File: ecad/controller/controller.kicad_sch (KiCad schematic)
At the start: 19 parts, among them J1 Conn_01x03_Pin, P1 USB_C_Plug_USB2.0, SW1 RST, SW2 BOOT, SW3 USER1, SW4 USER2, U1 ESP32-S3-WROOM-1, U2 AMS1117-3.3, U3 SN74LVC1T45DBV

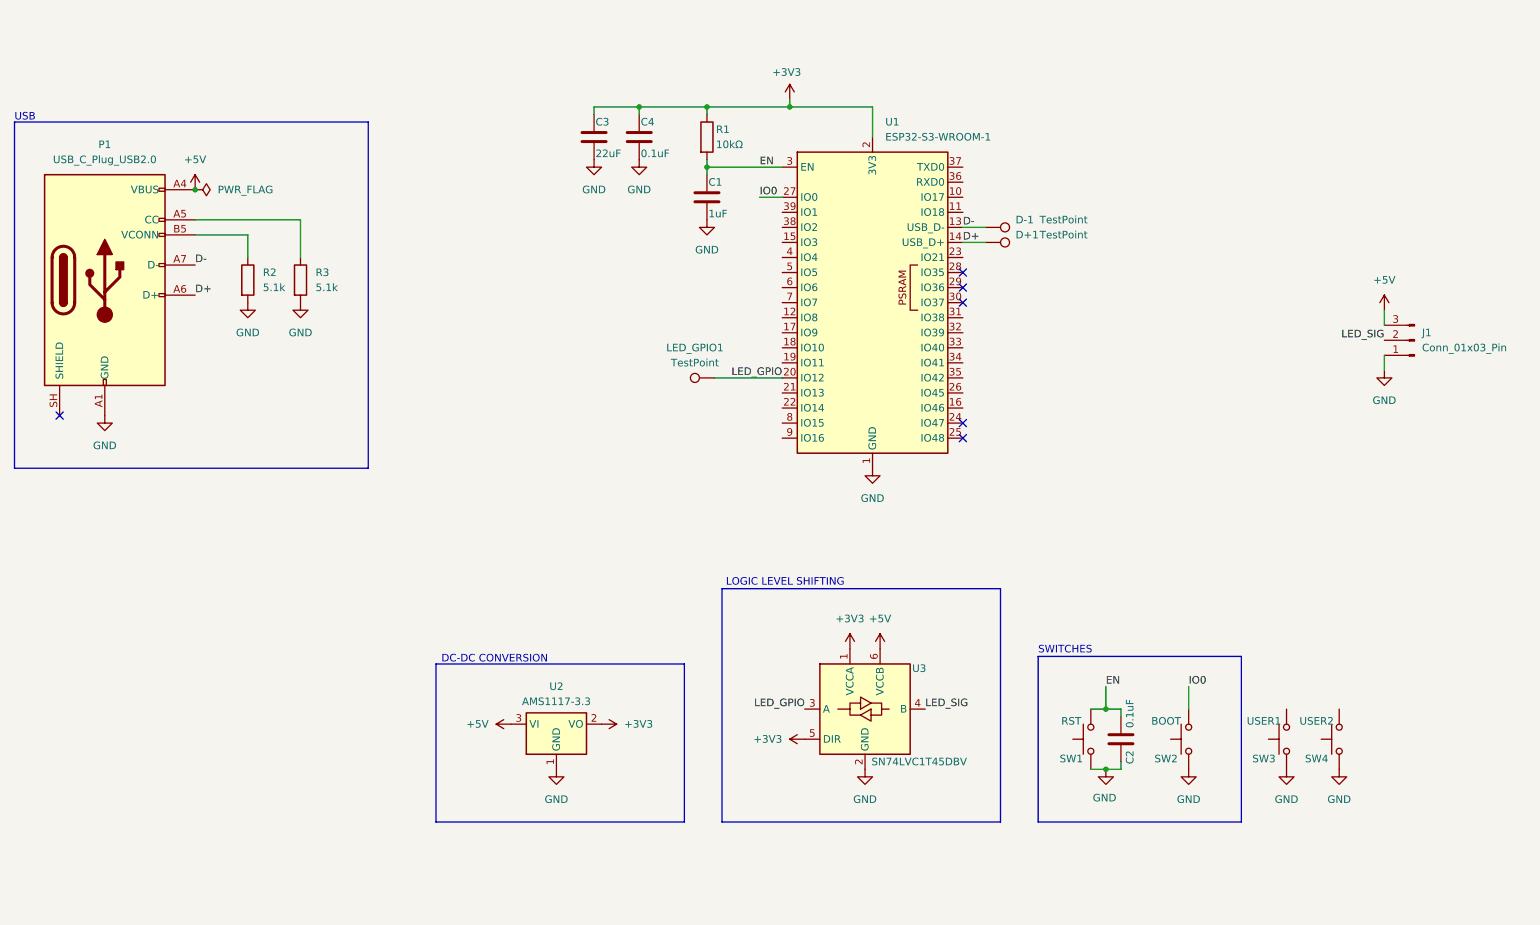
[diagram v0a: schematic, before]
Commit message: split into 2 boards; switch led panel from 4 layers to 2 layers;
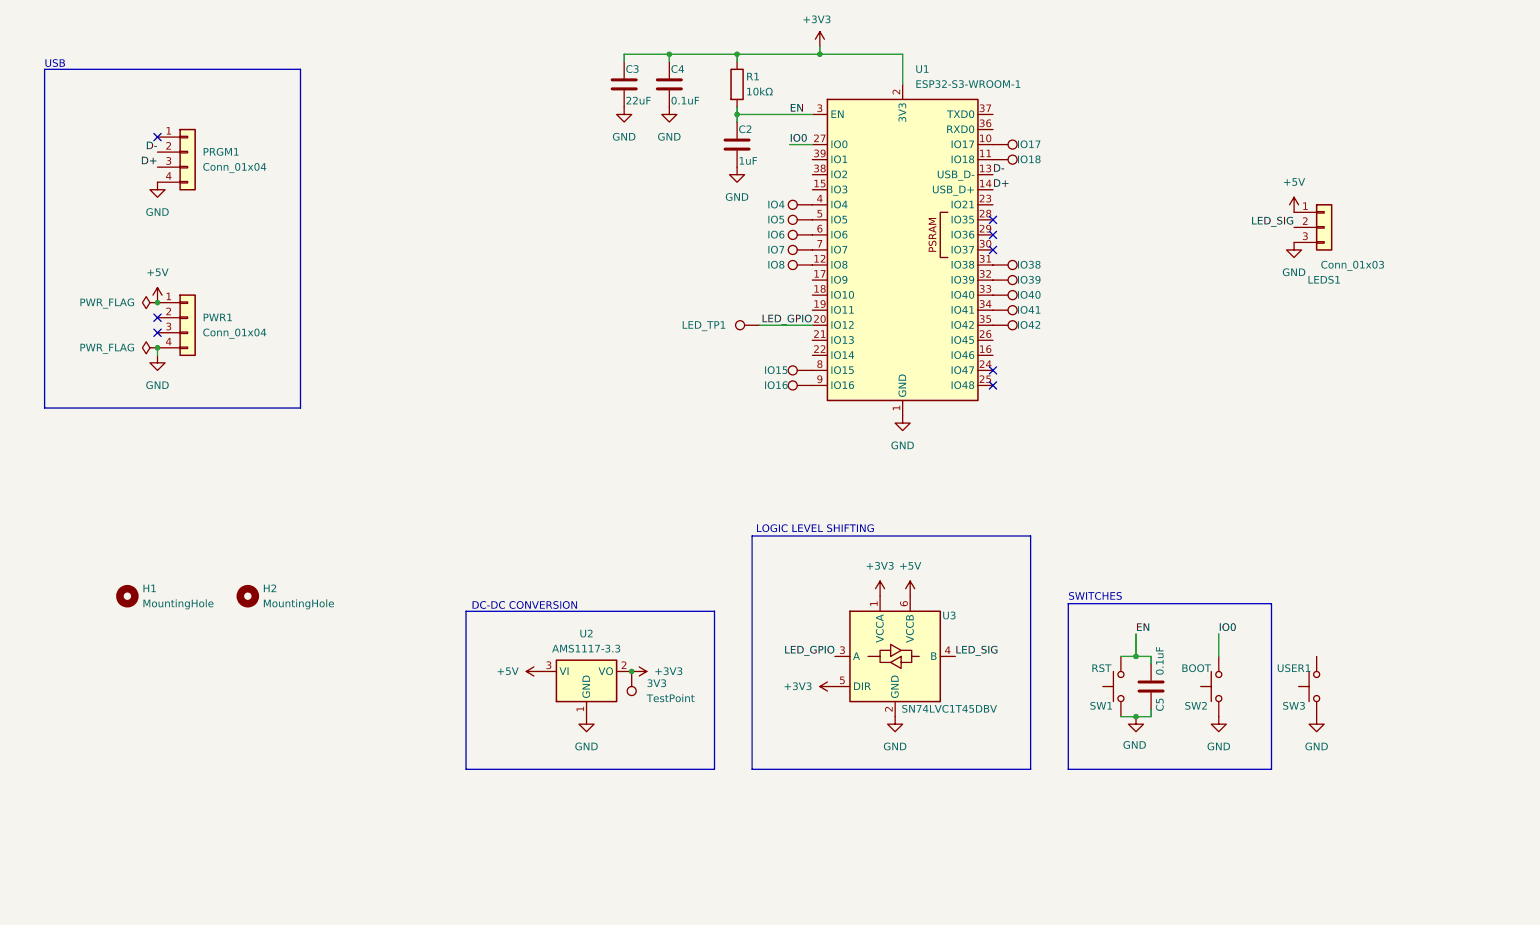
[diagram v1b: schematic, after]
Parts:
- removed C1: 1uF, Capacitor_SMD:C_0805_2012Metric, symbol Device:C
- removed D+1, D-1, LED_GPIO1: TestPoint, symbol Connector:TestPoint
- removed J1: Conn_01x03_Pin, symbol Connector:Conn_01x03_Pin
- removed P1: USB_C_Plug_USB2.0, Connector_USB:USB_C_Receptacle_HRO_TYPE-C-31-M-17, symbol Connector:USB_C_Plug_USB2.0
- removed R2, R3: 5.1k, Resistor_SMD:R_0805_2012Metric, symbol Device:R
- removed SW4: USER2, Button_Switch_THT:SW_PUSH_6mm, symbol Switch:SW_Push
- added 3V3, IO15, IO16, IO17, IO18, IO38, IO39, IO4, IO40, IO41, IO42, IO5, IO6, IO7, IO8, LED_TP1: TestPoint, TestPoint:TestPoint_Pad_D1.5mm, symbol Connector:TestPoint
- added C5: 0.1uF, Capacitor_SMD:C_0805_2012Metric, symbol Device:C
- added H1, H2: MountingHole, MountingHole:MountingHole_3.2mm_M3_Pad, symbol Mechanical:MountingHole
- added LEDS1: Conn_01x03, Connector_JST:JST_XH_B3B-XH-AM_1x03_P2.50mm_Vertical, symbol Connector_Generic:Conn_01x03
- added PRGM1, PWR1: Conn_01x04, Connector_JST:JST_XH_B4B-XH-AM_1x04_P2.50mm_Vertical, symbol Connector_Generic:Conn_01x04
- C2: value 0.1uF -> 1uF; KiLib_Generator (none) -> SMD_2terminal_chip_molded
- C3, C4, R1: KiLib_Generator (none) -> SMD_2terminal_chip_molded
- SW1, SW2: footprint Button_Switch_THT:SW_PUSH_6mm -> Button_Switch_SMD:SW_SPST_TS-1088-xR020
- SW3: footprint Button_Switch_THT:SW_PUSH_6mm -> Connector_JST:JST_XH_B3B-XH-AM_1x03_P2.50mm_Vertical; KiLib_Generator (none) -> connector/JST
- U3: KiLib_Generator (none) -> package/gullwing
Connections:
- net +3V3: now also 3V3.1
- net +5V: now also LEDS1.1 (Pin_1), PWR1.1 (Pin_1)
- net D+: now also PRGM1.3 (Pin_3)
- net D-: now also PRGM1.2 (Pin_2)
- net EN: now also C5.1
- net GND: now also C5.2, LEDS1.3 (Pin_3), PRGM1.4 (Pin_4), PWR1.4 (Pin_4)
- net LED_GPIO: now also LED_TP1.1
- net LED_SIG: now also LEDS1.2 (Pin_2)
- net at U1.10 (IO17): now also IO17.1
- net at U1.11 (IO18): now also IO18.1
- net at U1.12 (IO8): now also IO8.1
- net at U1.31 (IO38): now also IO38.1
- net at U1.32 (IO39): now also IO39.1
- net at U1.33 (IO40): now also IO40.1
- net at U1.34 (IO41): now also IO41.1
- net at U1.35 (IO42): now also IO42.1
- net at U1.4 (IO4): now also IO4.1
- net at U1.5 (IO5): now also IO5.1
- net at U1.6 (IO6): now also IO6.1
- net at U1.7 (IO7): now also IO7.1
- net at U1.8 (IO15): now also IO15.1
- net at U1.9 (IO16): now also IO16.1
- no-connect marks 6 -> 8

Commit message: added vertical USB-C connector to controller board; and possibly much more
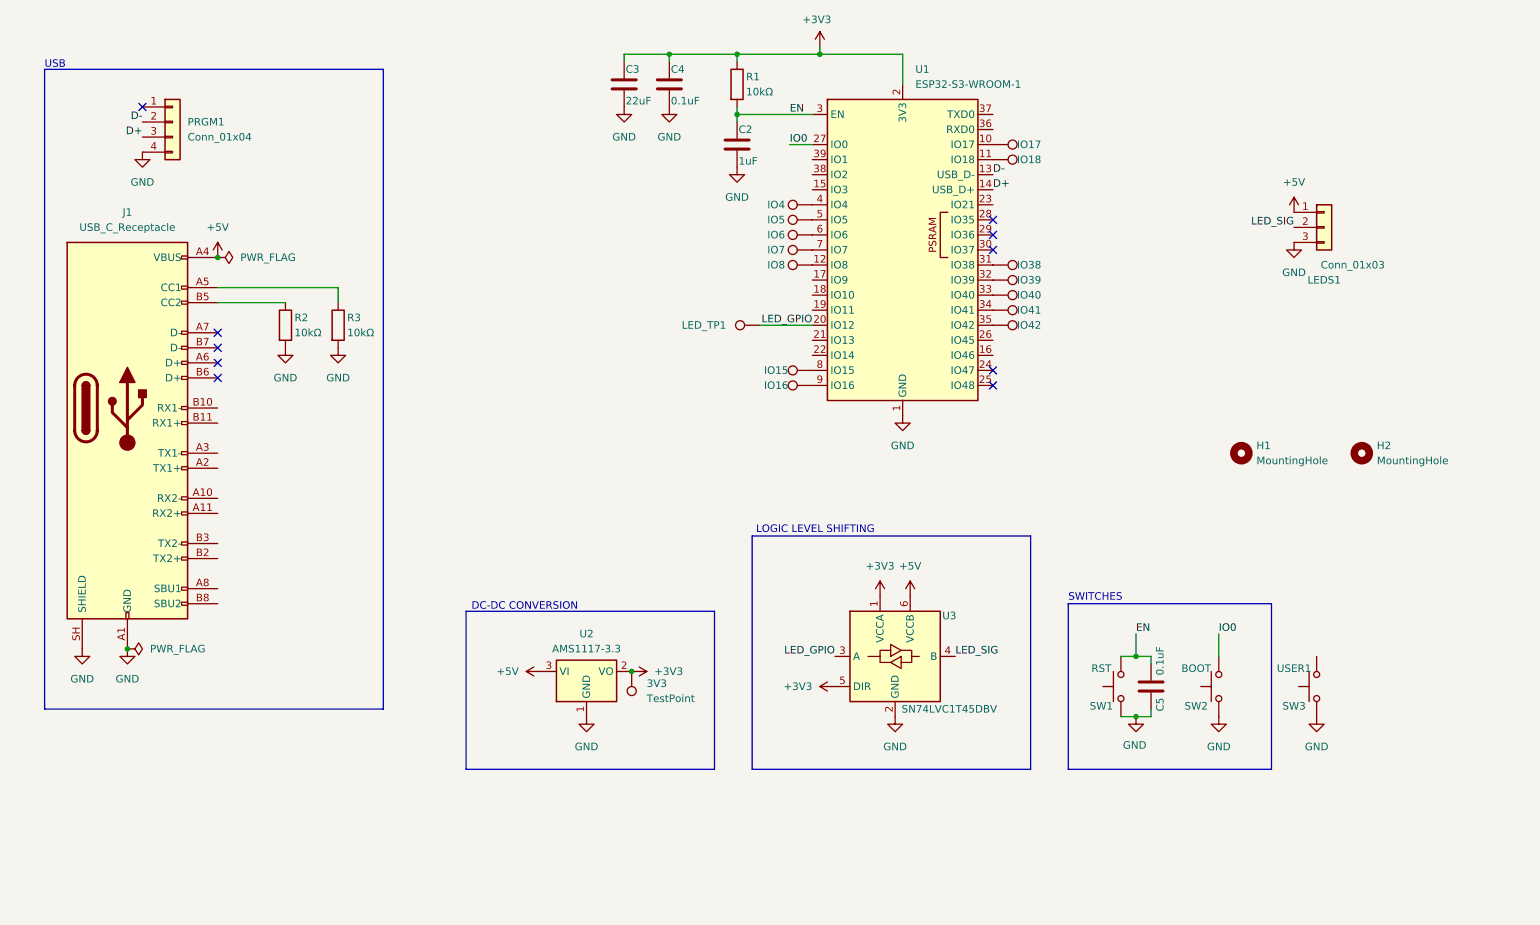
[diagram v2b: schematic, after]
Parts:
- removed PWR1: Conn_01x04, Connector_JST:JST_XH_B4B-XH-AM_1x04_P2.50mm_Vertical, symbol Connector_Generic:Conn_01x04
- added J1: USB_C_Receptacle, usb-library:USB-C-VERTICAL-14P, symbol Connector:USB_C_Receptacle
- added R2, R3: 10kΩ, Resistor_SMD:R_0805_2012Metric, symbol Device:R
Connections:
- net +5V: now also J1.A4 (VBUS), J1.A9 (VBUS), J1.B4 (VBUS), J1.B9 (VBUS)
- net GND: now also J1.A1 (GND), J1.A12 (GND), J1.B1 (GND), J1.B12 (GND), J1.SH (SHIELD), R2.2, R3.2
- new net: J1.A5 (CC1), R3.1
- new net: J1.B5 (CC2), R2.1
- no-connect marks 8 -> 10
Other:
- moved on the sheet: H1, H2, PRGM1

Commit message: who knows
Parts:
- SW3: footprint Connector_JST:JST_XH_B3B-XH-AM_1x03_P2.50mm_Vertical -> Button_Switch_SMD:SW_Push_1P1T_NO_E-Switch_TL3301NxxxxxG
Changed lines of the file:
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@@
 			)
 		)
-		(property "Footprint" "Connector_JST:JST_XH_B3B-XH-AM_1x03_P2.50mm_Vertical"
+		(property "Footprint" "Button_Switch_SMD:SW_Push_1P1T_NO_E-Switch_TL3301NxxxxxG"
 			(at 237.49 137.16 0)
 			(hide yes)

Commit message: add ESD protection; change USB connectors; ajust ESP32 pinout; more
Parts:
- removed J1: USB_C_Receptacle, usb-library:USB-C-VERTICAL-14P, symbol Connector:USB_C_Receptacle
- removed PRGM1: Conn_01x04, Connector_JST:JST_XH_B4B-XH-AM_1x04_P2.50mm_Vertical, symbol Connector_Generic:Conn_01x04
- added D1: SMAJ5.0CA, Diode_SMD:D_SMA, symbol Diode:SMAJ5.0CA
- added H3: MountingHole, MountingHole:MountingHole_3.2mm_M3, symbol Mechanical:MountingHole
- added J2: USB_C_Receptacle_PowerOnly_6P, usb-c:usb-c-vertical-smd, symbol Connector:USB_C_Receptacle_PowerOnly_6P
- added PRGM1: Conn_01x03, Connector_JST:JST_XH_B3B-XH-AM_1x03_P2.50mm_Vertical, symbol Connector_Generic:Conn_01x03
- added R4: 10kΩ, Resistor_SMD:R_0805_2012Metric, symbol Device:R
- added RXD0, TXD0: TestPoint, TestPoint:TestPoint_Pad_D1.5mm, symbol Connector:TestPoint
- added U4: USBLC6-2SC6, Package_TO_SOT_SMD:SOT-23-6, symbol Power_Protection:USBLC6-2SC6
- H1, H2: footprint MountingHole:MountingHole_3.2mm_M3_Pad -> MountingHole:MountingHole_3.2mm_M3
- R2, R3: value 10kΩ -> 5.1kΩ
- SW3: footprint Button_Switch_SMD:SW_Push_1P1T_NO_E-Switch_TL3301NxxxxxG -> Button_Switch_SMD:SW_SPST_TS-1088-xR020
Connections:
- net +3V3: now also R4.1
- net +5V: now also D1.2 (A2), J2.A9 (VBUS), J2.B9 (VBUS)
- net GND: now also D1.1 (A1), J2.A12 (GND), J2.B12 (GND), J2.SH (SHIELD), PRGM1.3 (Pin_3), U4.2 (GND)
- net SWITCH: now reaches SW3.2
- net SWITCH: now also U1.17 (IO9), R4.2
- net at R3.1: now also J2.A5 (CC1)
- net at R2.1: now also J2.B5 (CC2)
- net at U1.36 (RXD0): now also RXD0.1
- net at U1.37 (TXD0): now also TXD0.1
- net D+ renamed USB_D+
- net USB_D+: now also U4.4 (I/O2)
- net D- renamed USB_D-
- net USB_D-: now also U4.6 (I/O1)
- new net IN_D+: PRGM1.1 (Pin_1), U4.3 (I/O2)
- new net IN_D-: PRGM1.2 (Pin_2), U4.1 (I/O1)
- no-connect marks 10 -> 12
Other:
- moved on the sheet: H1, H2, R2, R3, SW3

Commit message: add decoupling caps; correct hole shape in usb-c footprint
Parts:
- added C7: 0.1uF, Capacitor_SMD:C_0805_2012Metric, symbol Device:C
- added C8, C9: 10uF, Capacitor_SMD:C_0805_2012Metric, symbol Device:C
- added R5: 10kΩ, Resistor_SMD:R_0805_2012Metric, symbol Device:R
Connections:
- net +3V3: now also C7.1, C8.1, R5.1
- net +5V: now also C9.1
- net GND: now also C7.2, C8.2, C9.2
- net IO0: now also R5.2
- no-connect marks 12 -> 16
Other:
- moved on the sheet: 3V3, U2

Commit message: populate BOM fields with MPN and LCSC Part #
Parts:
- 3V3, IO15, IO16, IO17, IO18, IO38, IO39, IO4, IO40, IO41, IO42, IO5, IO6, IO7, IO8, LED_TP1, RXD0, TXD0: now left out of the parts list
- C2: LCSC# (none) -> C28323; MPN (none) -> CL21B105KBFNNNE
- C3: LCSC# (none) -> C86816; MPN (none) -> GRM21BR61E226ME44L
- C4, C5, C7: LCSC# (none) -> C1711; MPN (none) -> CL21B104KBCNNNC
- C8, C9: LCSC# (none) -> C15850; MPN (none) -> CL21A106KAYNNNE
- D1: LCSC# (none) -> C83324; MPN (none) -> SMAJ5.0CA
- J2: LCSC# (none) -> C5156600; MPN (none) -> TYPE-C 6PLTH6.8-DJ
- LEDS1, PRGM1: LCSC# (none) -> C144394; MPN (none) -> B3B-XH-A(LF)(SN)
- R1, R4, R5: LCSC# (none) -> C2907219; MPN (none) -> FRC0805F1002TS
- R2, R3: LCSC# (none) -> C84375; MPN (none) -> RC0805FR-075K1L
- SW1: value RST -> SW; LCSC# (none) -> C720477; MPN (none) -> TS-1088-AR02016
- SW2: value BOOT -> SW; LCSC# (none) -> C720477; MPN (none) -> TS-1088-AR02016
- SW3: value USER1 -> SW; LCSC# (none) -> C720477; MPN (none) -> TS-1088-AR02016
- U1: LCSC# (none) -> C2913202; MPN (none) -> ESP32-S3-WROOM-1-N16R8
- U2: LCSC# (none) -> C6186; MPN (none) -> AMS1117-3.3
- U3: LCSC# (none) -> C7843; MPN (none) -> SN74LVC1T45DBVR
- U4: LCSC# (none) -> C7519; MPN (none) -> USBLC6-2SC6

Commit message: final design review for v1 order; reroute some components; add LED to controller
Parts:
- removed 3V3, IO18, IO8: TestPoint, TestPoint:TestPoint_Pad_D1.5mm, symbol Connector:TestPoint
- removed C8: 10uF, Capacitor_SMD:C_0805_2012Metric, symbol Device:C
- added D2: LED, LED_SMD:LED_0805_2012Metric_Pad1.15x1.40mm_HandSolder, symbol Device:LED
- added H4: MountingHole, MountingHole:MountingHole_3.2mm_M3_DIN965_Pad_TopOnly, symbol Mechanical:MountingHole
- added R6: 50Ω, Resistor_SMD:R_0805_2012Metric, symbol Device:R
- H1, H2, H3: footprint MountingHole:MountingHole_3.2mm_M3 -> MountingHole:MountingHole_3.2mm_M3_DIN965_Pad_TopOnly
- PRGM1: footprint Connector_JST:JST_XH_B3B-XH-AM_1x03_P2.50mm_Vertical -> Connector_PinHeader_2.54mm:PinHeader_1x03_P2.54mm_Vertical; LCSC# C144394 -> C52016391; MPN B3B-XH-A(LF)(SN) -> HX PH254-01-03-Z-L11.5 pcb pin header
- U3, U4: footprint Package_TO_SOT_SMD:SOT-23-6 -> Package_TO_SOT_SMD:SOT-23-6_Handsoldering
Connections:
- net GND: now also D2.1 (K)
- net at IO17.1, U1.10 (IO17): now also R6.1
- new net: D2.2 (A), R6.2
- no-connect marks 16 -> 18
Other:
- moved on the sheet: C7, H1, H2, H3, IO17
